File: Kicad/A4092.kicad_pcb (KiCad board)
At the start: 4 copper layers, 175.6 x 122.1 mm, 107 parts, among them CN1 Zorro3, J1 Conn_02x25_Odd_Even, J2 Conn_01x06_Pin, J3 TO-LED, J4 TO-MB, J5 5787170-5, J7 22112042, J8 TO-A3000-LED, J9 TO-A3000-MB, SW1 219-8MST, U1 SN74ABT16543DGGR, U10 NCR53c710 SCSI Host Controller, U11 DS21S07A, U12 DS21S07A, U13 SST39SF010/020/040, U2 SN74ABT16543DGGR, U3 SN74ABT16543DGGR, U4 SN74ABT16543DGGR, U5 74LVC07APW_118, U6 SN74ABT16245ADGGR, U7 AMS1117-3.3, U8 SN74F244DB, U9 XC95144XL-TQ144, Y1 Abracon ACO-50MHz

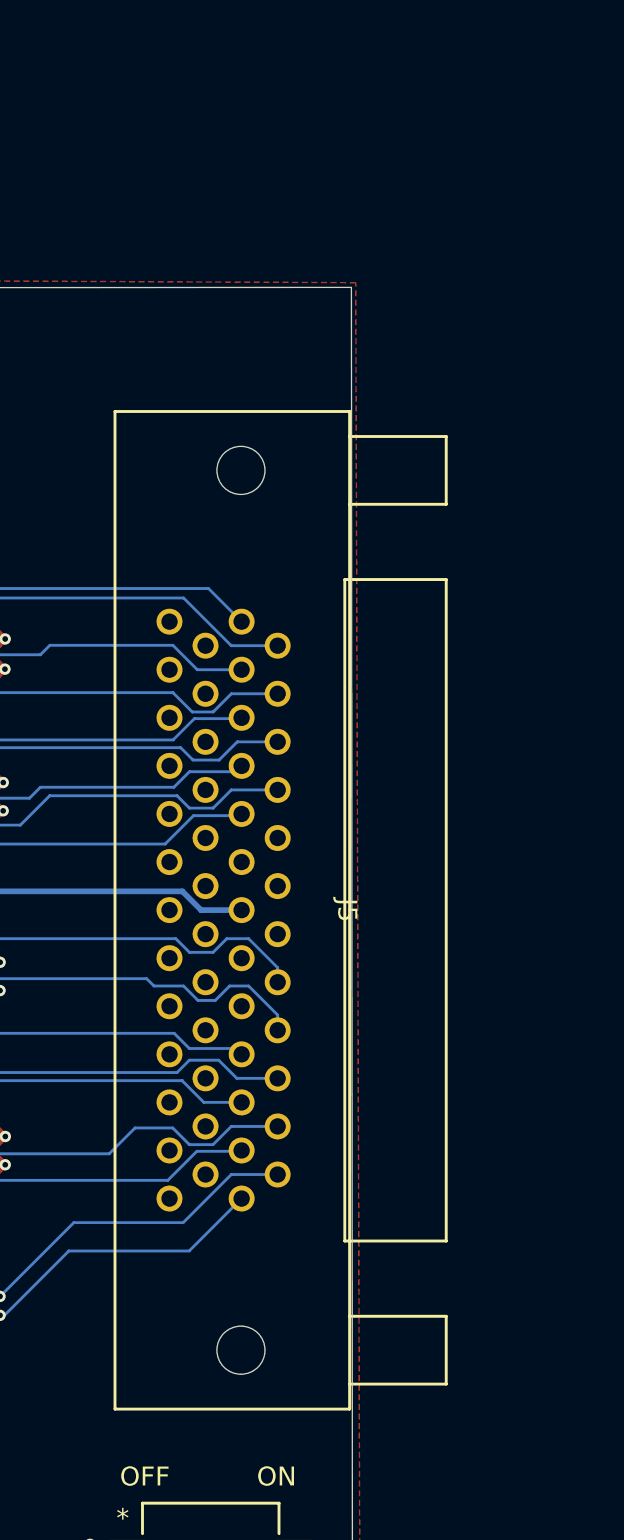
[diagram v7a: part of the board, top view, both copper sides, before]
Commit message: Move HPDB50 connector to back panel
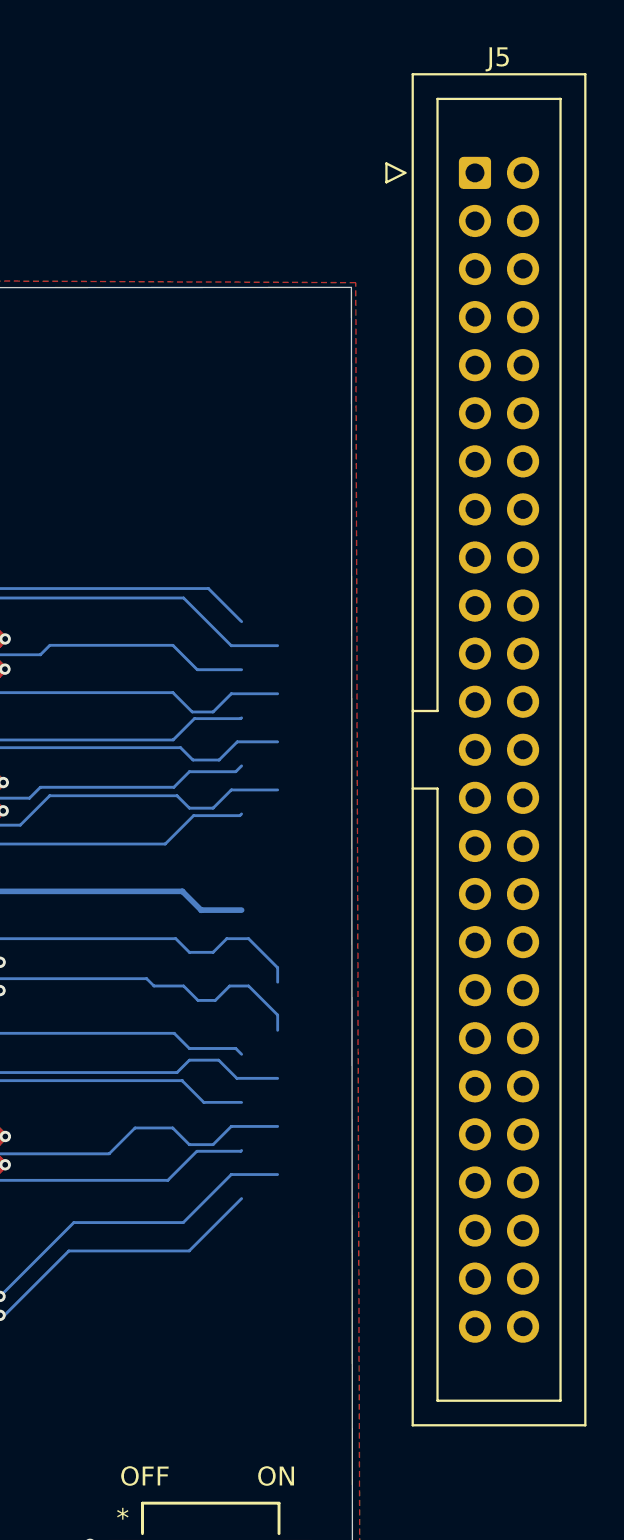
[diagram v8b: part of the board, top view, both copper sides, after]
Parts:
- J5: value 5787170-5 -> Conn_02x25_Odd_Even; footprint 5787170_5:CONN_5787170-5_TYC -> kicad-official/Connector_IDC.pretty:IDC-Header_2x25_P2.54mm_Vertical
- moved J5 25.9 mm to (231.0, 26.5), turned to 0 degrees
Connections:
- C10 pad 4: Net-(C10-Pad4) -> Net-(J5-Pin_48)
- C6 pad 1: Net-(C6-Pad1) -> Net-(J5-Pin_2)
- C6 pad 2: Net-(C6-Pad2) -> Net-(J5-Pin_4)
- C6 pad 3: Net-(C6-Pad3) -> Net-(J5-Pin_6)
- C6 pad 4: Net-(C6-Pad4) -> Net-(J5-Pin_8)
- C7 pad 1: Net-(C7-Pad1) -> Net-(J5-Pin_10)
- C7 pad 2: Net-(C7-Pad2) -> Net-(J5-Pin_12)
- C7 pad 3: Net-(C7-Pad3) -> Net-(J5-Pin_14)
- C7 pad 4: Net-(C7-Pad4) -> Net-(J5-Pin_16)
- C8 pad 1: Net-(C8-Pad1) -> Net-(J5-Pin_18)
- C8 pad 2: Net-(C8-Pad2) -> Net-(J5-Pin_32)
- C8 pad 3: Net-(C8-Pad3) -> Net-(J5-Pin_36)
- C8 pad 4: Net-(C8-Pad4) -> Net-(J5-Pin_38)
- C9 pad 1: Net-(C9-Pad1) -> Net-(J5-Pin_40)
- C9 pad 2: Net-(C9-Pad2) -> Net-(J5-Pin_42)
- C9 pad 3: Net-(C9-Pad3) -> Net-(J5-Pin_44)
- C9 pad 4: Net-(C9-Pad4) -> Net-(J5-Pin_46)
- FL10 pad 5: Net-(C6-Pad4) -> Net-(J5-Pin_8)
- FL10 pad 6: Net-(C6-Pad3) -> Net-(J5-Pin_6)
- FL10 pad 7: Net-(C6-Pad2) -> Net-(J5-Pin_4)
- FL10 pad 8: Net-(C6-Pad1) -> Net-(J5-Pin_2)
- FL6 pad 5: Net-(C9-Pad4) -> Net-(J5-Pin_46)
- FL6 pad 6: Net-(C9-Pad3) -> Net-(J5-Pin_44)
- FL6 pad 7: Net-(C9-Pad2) -> Net-(J5-Pin_42)
- FL6 pad 8: Net-(C9-Pad1) -> Net-(J5-Pin_40)
- FL7 pad 8: Net-(C10-Pad4) -> Net-(J5-Pin_48)
- FL8 pad 5: Net-(C8-Pad4) -> Net-(J5-Pin_38)
- FL8 pad 6: Net-(C8-Pad3) -> Net-(J5-Pin_36)
- FL8 pad 7: Net-(C8-Pad2) -> Net-(J5-Pin_32)
- FL8 pad 8: Net-(C8-Pad1) -> Net-(J5-Pin_18)
- FL9 pad 5: Net-(C7-Pad4) -> Net-(J5-Pin_16)
- FL9 pad 6: Net-(C7-Pad3) -> Net-(J5-Pin_14)
- FL9 pad 7: Net-(C7-Pad2) -> Net-(J5-Pin_12)
- FL9 pad 8: Net-(C7-Pad1) -> Net-(J5-Pin_10)
- J5 pad 10: GND -> Net-(J5-Pin_10)
- J5 pad 12: unconnected-(J5-Pad12) -> Net-(J5-Pin_12)
- J5 pad 13: unconnected-(J5-Pad13) -> GND
- J5 pad 14: unconnected-(J5-Pad14) -> Net-(J5-Pin_14)
- J5 pad 16: GND -> Net-(J5-Pin_16)
- J5 pad 18: GND -> Net-(J5-Pin_18)
- J5 pad 2: GND -> Net-(J5-Pin_2)
- J5 pad 25: GND -> unconnected-(J5-Pin_25-Pad25)
- J5 pad 26: Net-(C6-Pad1) -> SCSI_TERMPWR
- J5 pad 27: Net-(C6-Pad2) -> GND
- J5 pad 28: Net-(C6-Pad3) -> GND
- J5 pad 29: Net-(C6-Pad4) -> GND
- J5 pad 30: Net-(C7-Pad1) -> GND
- J5 pad 31: Net-(C7-Pad2) -> GND
- J5 pad 32: Net-(C7-Pad3) -> Net-(J5-Pin_32)
- J5 pad 33: Net-(C7-Pad4) -> GND
- J5 pad 34: Net-(C8-Pad1) -> unconnected-(J5-Pin_34-Pad34)
- J5 pad 36: GND -> Net-(J5-Pin_36)
- J5 pad 37: unconnected-(J5-Pad37) -> GND
- J5 pad 38: SCSI_TERMPWR -> Net-(J5-Pin_38)
- J5 pad 39: unconnected-(J5-Pad39) -> GND
- J5 pad 4: GND -> Net-(J5-Pin_4)
- J5 pad 40: GND -> Net-(J5-Pin_40)
- J5 pad 41: Net-(C8-Pad2) -> GND
- J5 pad 42: GND -> Net-(J5-Pin_42)
- J5 pad 43: Net-(C8-Pad3) -> GND
- J5 pad 44: Net-(C8-Pad4) -> Net-(J5-Pin_44)
- J5 pad 45: Net-(C9-Pad1) -> GND
- J5 pad 46: Net-(C9-Pad2) -> Net-(J5-Pin_46)
- J5 pad 47: Net-(C9-Pad3) -> GND
- J5 pad 48: Net-(C9-Pad4) -> Net-(J5-Pin_48)
- J5 pad 49: Net-(C10-Pad4) -> GND
- J5 pad 6: GND -> Net-(J5-Pin_6)
- J5 pad 8: GND -> Net-(J5-Pin_8)
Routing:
- net Net-(J5-Pin_48): track 0.00 -> 26.2 mm, vias 0 -> 2
- net Net-(C10-Pad4): track 26.2 -> 0.00 mm, vias 2 -> 0
- net Net-(J5-Pin_18): track 0.00 -> 25.9 mm, vias 0 -> 1
- net Net-(C8-Pad1): track 25.9 -> 0.00 mm, vias 1 -> 0
- net Net-(J5-Pin_36): track 0.00 -> 25.9 mm, vias 0 -> 1
- net Net-(C8-Pad3): track 25.9 -> 0.00 mm, vias 1 -> 0
- net Net-(J5-Pin_32): track 0.00 -> 25.5 mm, vias 0 -> 1
- net Net-(C8-Pad2): track 25.5 -> 0.00 mm, vias 1 -> 0
- net Net-(J5-Pin_4): track 0.00 -> 25.1 mm, vias 0 -> 1
- net Net-(C6-Pad2): track 25.1 -> 0.00 mm, vias 1 -> 0
- net Net-(J5-Pin_40): track 0.00 -> 25.0 mm, vias 0 -> 1
- net Net-(C9-Pad1): track 25.0 -> 0.00 mm, vias 1 -> 0
- net Net-(J5-Pin_12): track 0.00 -> 24.7 mm, vias 0 -> 1
- net Net-(C7-Pad2): track 24.7 -> 0.00 mm, vias 1 -> 0
- net Net-(J5-Pin_16): track 0.00 -> 24.7 mm, vias 0 -> 1
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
